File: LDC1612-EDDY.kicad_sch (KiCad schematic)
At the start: 10 parts, among them J1 Conn_01x04_Pin, J2 Conn_01x02_Pin, U1 LDC1612, U2 XC6206P332MR

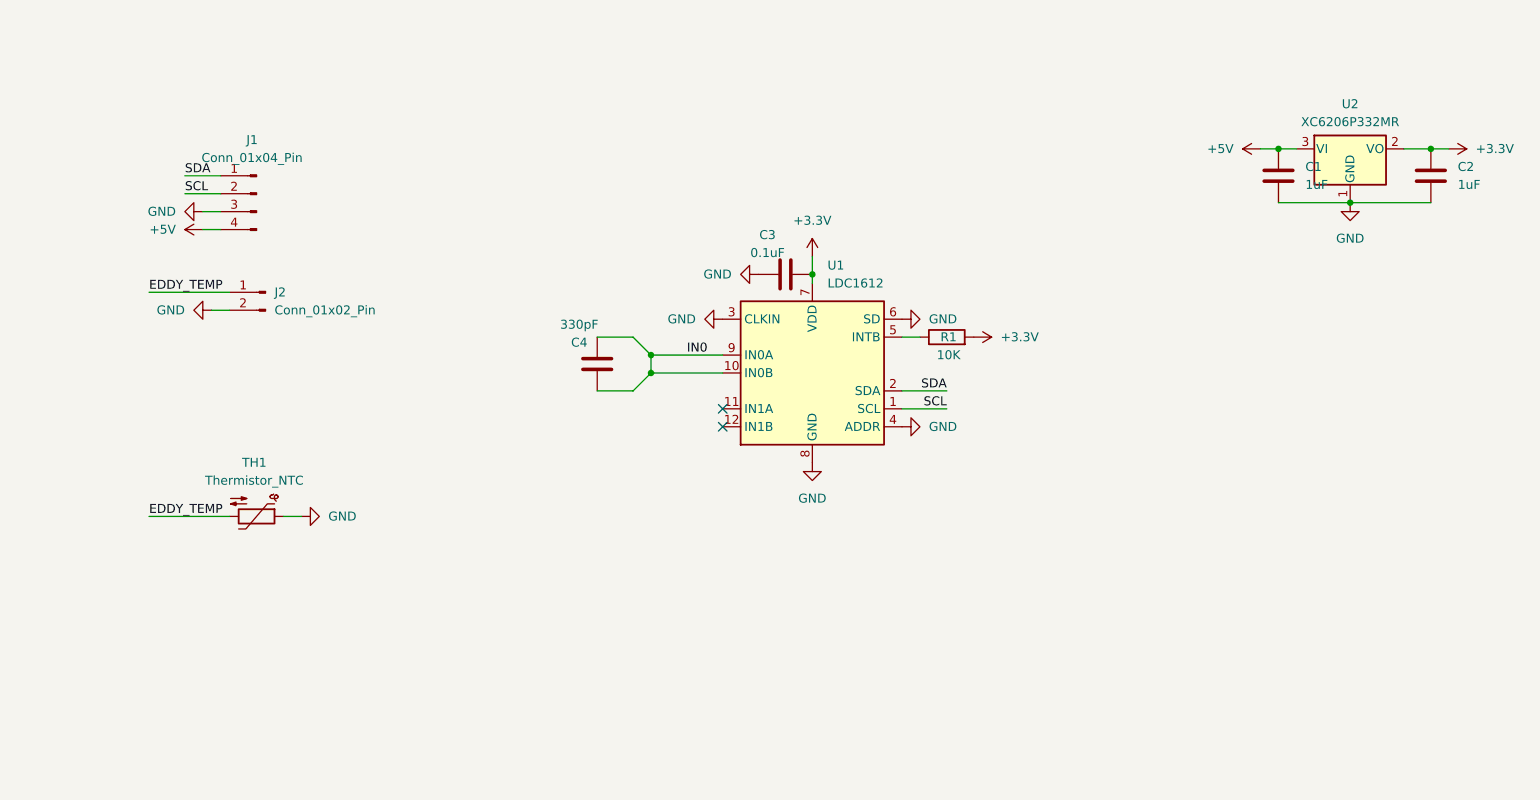
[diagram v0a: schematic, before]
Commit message: Schematic: add pull-up resistors for I2C SDA & SCL also make groups for different sections
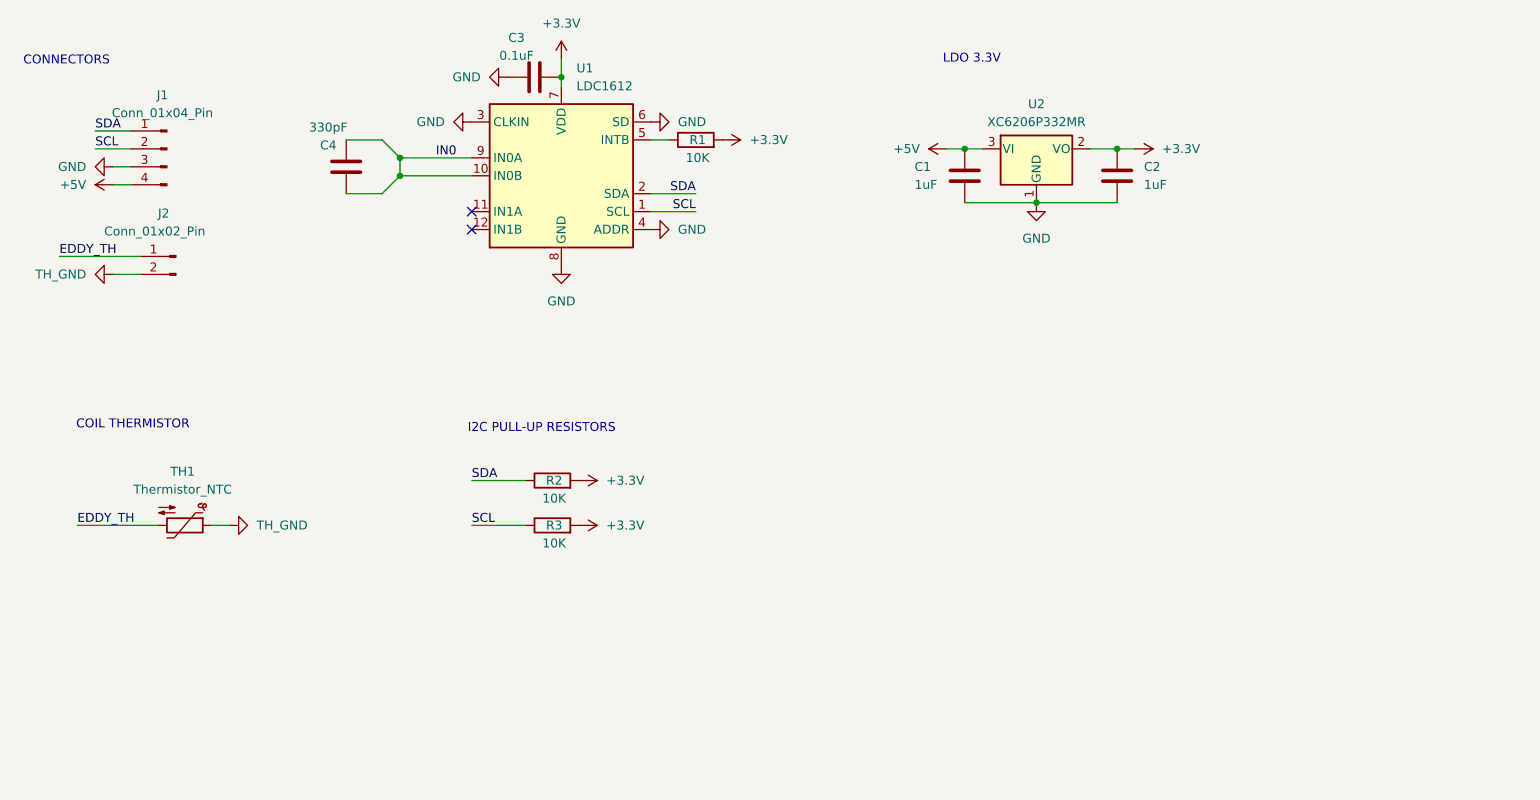
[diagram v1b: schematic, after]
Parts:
- added R2, R3: 10K, Resistor_SMD:R_0402_1005Metric_Pad0.72x0.64mm_HandSolder, symbol Device:R
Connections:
- net +3.3V: now also R2.2, R3.2
- net GND: no longer J2.2 (Pin_2), TH1.1
- net SCL: now also R3.1
- net SDA: now also R2.1
- net EDDY_TEMP renamed EDDY_TH
- new net TH_GND: J2.2 (Pin_2), TH1.1
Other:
- note added: "COIL THERMISTOR"
- note added: "CONNECTORS"
- note added: "I2C PULL-UP RESISTORS"
- note added: "LDO 3.3V"
- moved on the sheet: C1, C2, C3, C4, J1, J2, R1, TH1, U1, U2

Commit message: Schematic & PCB: bump version to v1.1 * added an 12MHz external oscillator * fixed LDC1612 GND pin does not connected
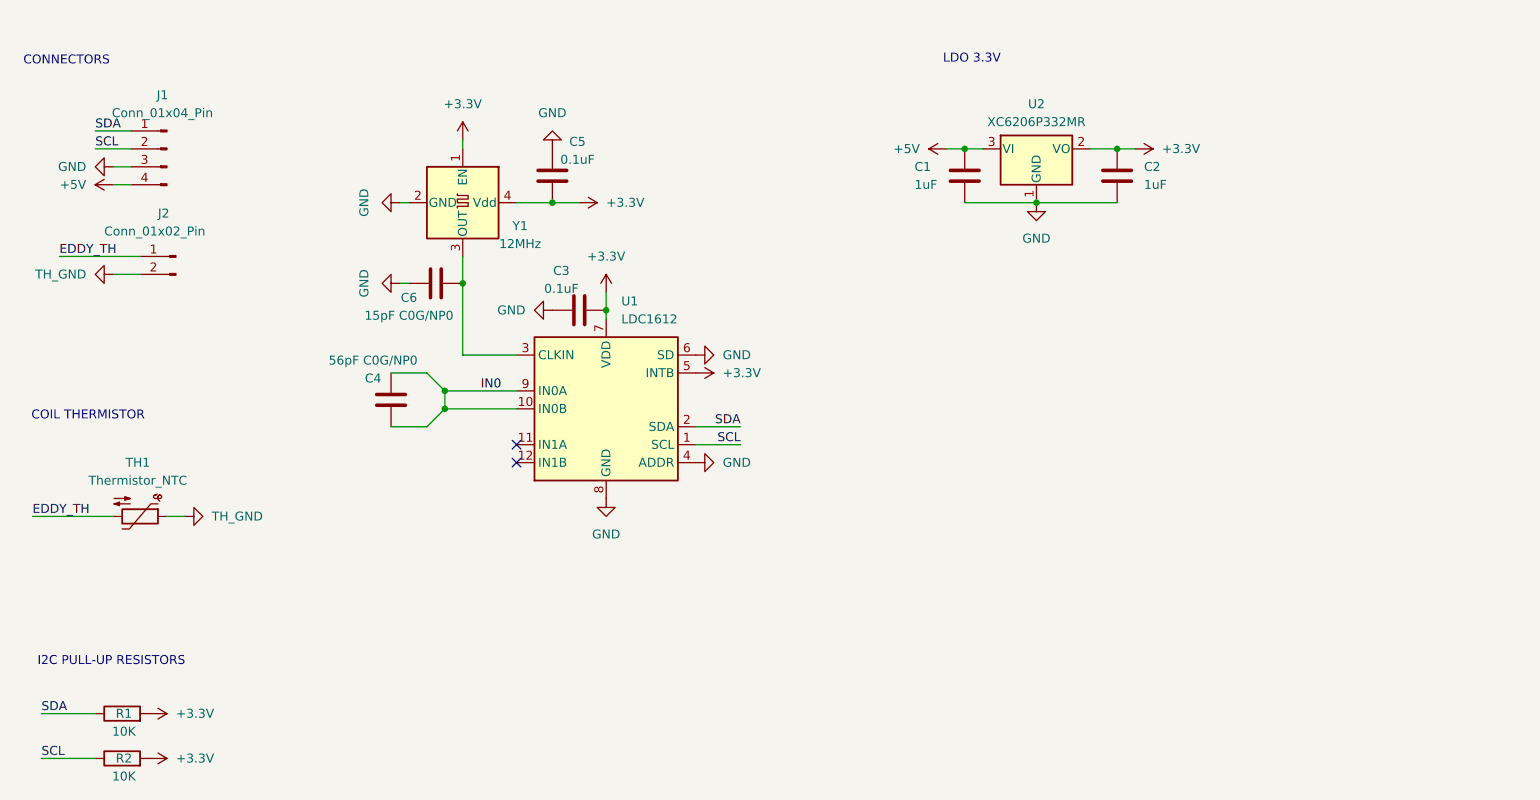
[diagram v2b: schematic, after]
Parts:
- removed R1: 10K, Resistor_SMD:R_0402_1005Metric_Pad0.72x0.64mm_HandSolder, symbol Device:R
- added C5: 0.1uF, Capacitor_SMD:C_0402_1005Metric_Pad0.74x0.62mm_HandSolder, symbol Device:C
- added C6: 15pF C0G/NP0, Capacitor_SMD:C_0402_1005Metric_Pad0.74x0.62mm_HandSolder, symbol Device:C
- added Y1: 12MHz, Oscillator:Oscillator_SMD_Abracon_ASCO-4Pin_1.6x1.2mm, symbol Oscillator:ASE-xxxMHz
- C4: value 330pF -> 56pF C0G/NP0; footprint Capacitor_SMD:C_0402_1005Metric_Pad0.74x0.62mm_HandSolder -> Capacitor_SMD:C_0402_1005Metric
- TH1: footprint Resistor_SMD:R_0603_1608Metric_Pad0.98x0.95mm_HandSolder -> Resistor_SMD:R_0603_1608Metric
- renumbered R2 to R1, R3 to R2
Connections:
- net +3.3V: now also U1.5 (INTB), C5.1, Y1.1 (EN), Y1.4 (Vdd)
- net GND: now also C5.2, C6.2, Y1.2 (GND); no longer U1.3 (CLKIN)
- new net: C6.1, U1.3 (CLKIN), Y1.3 (OUT)
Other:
- moved on the sheet: C3, C4, R1, R2, TH1, U1

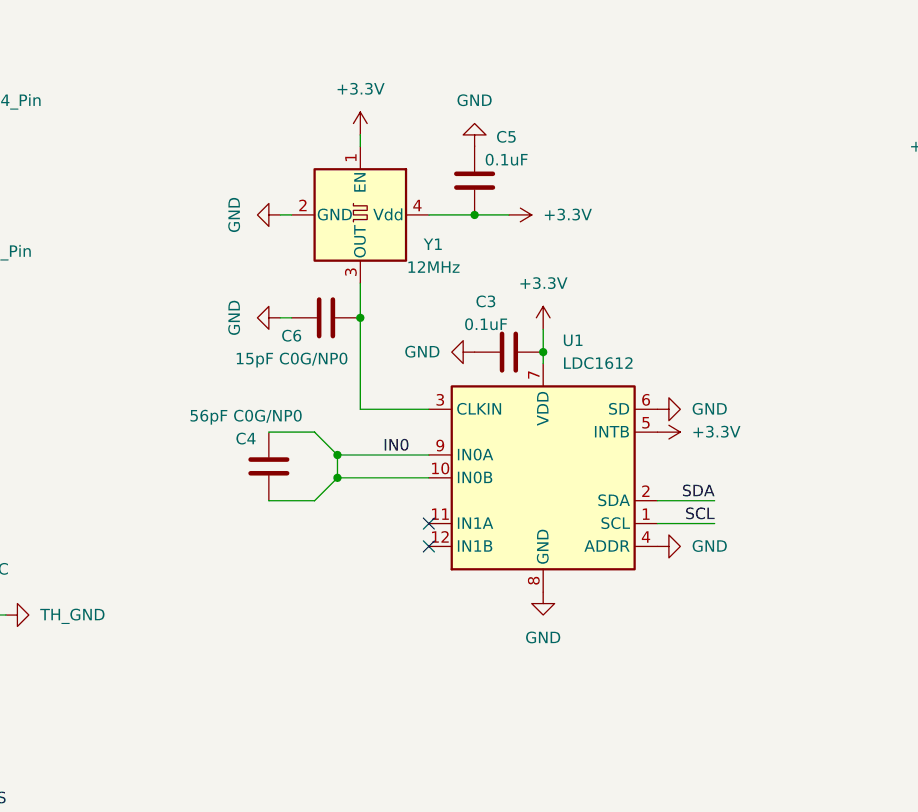
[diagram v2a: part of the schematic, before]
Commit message: release no oscillator version
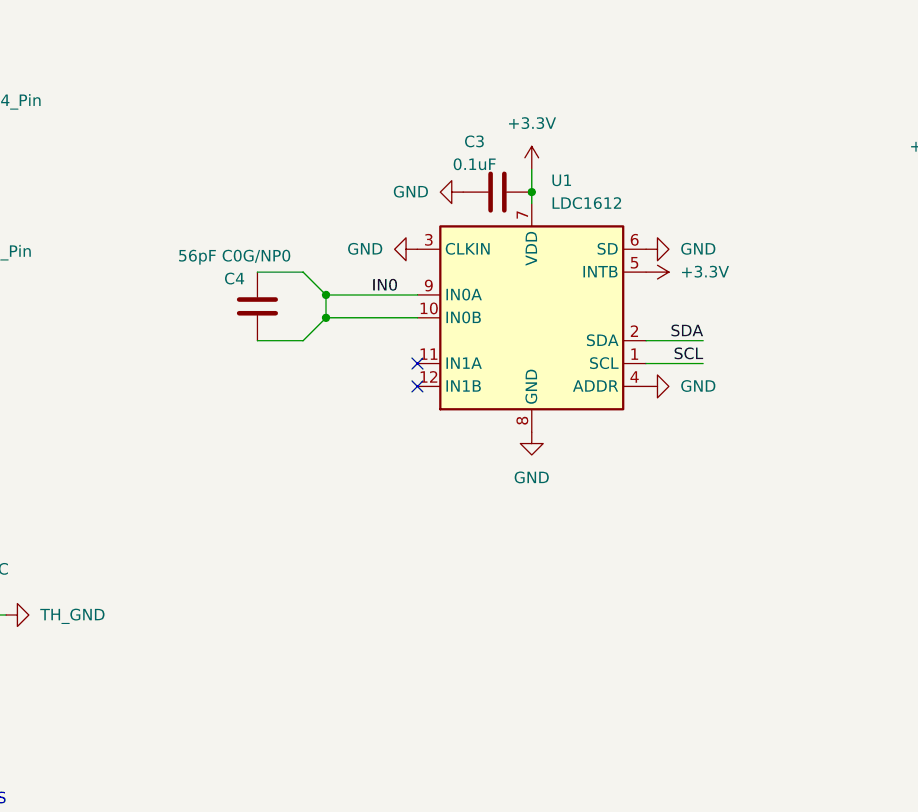
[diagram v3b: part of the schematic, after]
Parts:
- removed C5: 0.1uF, Capacitor_SMD:C_0402_1005Metric_Pad0.74x0.62mm_HandSolder, symbol Device:C
- removed C6: 15pF C0G/NP0, Capacitor_SMD:C_0402_1005Metric_Pad0.74x0.62mm_HandSolder, symbol Device:C
- removed Y1: 12MHz, Oscillator:Oscillator_SMD_Abracon_ASCO-4Pin_1.6x1.2mm, symbol Oscillator:ASE-xxxMHz
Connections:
- net GND: now also U1.3 (CLKIN)
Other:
- moved on the sheet: C3, C4, U1
